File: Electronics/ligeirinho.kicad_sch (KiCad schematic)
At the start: 18 parts, among them J1 VS1838B, J10 ponte H, J11 ponte H ld motores, J12 MPU6050, J2 motor B, J3 motor A, J4 Conn_01x15, J5 VL53L0X 1, J6 VL53L0X 2, J7 VL53L0X 3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

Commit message: shore: update electronic repository
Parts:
- removed BT1: Battery_Cell, symbol Device:Battery_Cell
- added J8: bateria, symbol Connector:Conn_01x02_Pin
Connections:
- net 2s: now also J8.1 (Pin_1)
- net GND: now also J8.2 (Pin_2)
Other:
- moved on the sheet: J2, J3
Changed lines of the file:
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@@
+    (stroke (width 0) (type default))
+  )
+  (wire (pts (xy 71.12 152.4) (xy 71.12 161.29))
     (stroke (width 0) (type default))
   )
@@
     (stroke (width 0) (type default))
   )
-  (wire (pts (xy 236.22 160.02) (xy 240.03 160.02))
+  (wire (pts (xy 236.22 160.02) (xy 242.57 160.02))
     (stroke (width 0) (type default) (color 0 0 0 1))
   )
@@
     (stroke (width 0) (type default))
   )
-  (wire (pts (xy 71.12 166.37) (xy 71.12 170.18))
+  (wire (pts (xy 71.12 163.83) (xy 71.12 170.18))
     (stroke (width 0) (type default))
   )
   (wire (pts (xy 93.98 170.18) (xy 105.41 170.18))
-    (stroke (width 0) (type default))
-  )
-  (wire (pts (xy 71.12 158.75) (xy 71.12 152.4))
     (stroke (width 0) (type default))
   )
@@
     )
   )
-  (global_label "2s" (shape input) (at 71.12 157.48 0) (fields_autoplaced)
-    (effects (font (size 1.27 1.27)) (justify left))
-    (property "Intersheetrefs" "${INTERSHEET_REFS}" (at 76.3428 157.48 0)
+  (global_label "2s" (shape input) (at 71.12 152.4 90) (fields_autoplaced)
+    (effects (font (size 1.27 1.27)) (justify left))
+    (property "Intersheetrefs" "${INTERSHEET_REFS}" (at 71.12 147.1772 90)
       (effects (font (size 1.27 1.27)) (justify left) hide)
     )
@@
     )
   )
-  (global_label "BO1" (shape input) (at 162.56 154.94 0) (fields_autoplaced)
-    (effects (font (size 1.27 1.27)) (justify left))
-    (property "Intersheetrefs" "${INTERSHEET_REFS}" (at 169.3552 154.94 0)
+  (global_label "BO1" (shape input) (at 171.45 157.48 0) (fields_autoplaced)
+    (effects (font (size 1.27 1.27)) (justify left))
+    (property "Intersheetrefs" "${INTERSHEET_REFS}" (at 178.2452 157.48 0)
       (effects (font (size 1.27 1.27)) (justify left) hide)
     )
@@
     )
   )
-  (global_label "GND" (shape input) (at 240.03 160.02 0) (fields_autoplaced)
-    (effects (font (size 1.27 1.27)) (justify left))
-    (property "Intersheetrefs" "${INTERSHEET_REFS}" (at 246.8857 160.02 0)
+  (global_label "GND" (shape input) (at 242.57 160.02 0) (fields_autoplaced)
+    (effects (font (size 1.27 1.27)) (justify left))
+    (property "Intersheetrefs" "${INTERSHEET_REFS}" (at 249.4257 160.02 0)
       (effects (font (size 1.27 1.27)) (justify left) hide)
     )
@@
     )
   )
-  (global_label "AO1" (shape input) (at 171.45 148.59 0) (fields_autoplaced)
-    (effects (font (size 1.27 1.27)) (justify left))
-    (property "Intersheetrefs" "${INTERSHEET_REFS}" (at 178.0638 148.59 0)
+  (global_label "AO1" (shape input) (at 171.45 143.51 0) (fields_autoplaced)
+    (effects (font (size 1.27 1.27)) (justify left))
+    (property "Intersheetrefs" "${INTERSHEET_REFS}" (at 178.0638 143.51 0)
       (effects (font (size 1.27 1.27)) (justify left) hide)
     )
@@
     )
   )
-  (global_label "AO2" (shape input) (at 171.45 151.13 0) (fields_autoplaced)
-    (effects (font (size 1.27 1.27)) (justify left))
-    (property "Intersheetrefs" "${INTERSHEET_REFS}" (at 178.0638 151.13 0)
-      (effects (font (size 1.27 1.27)) (justify left) hide)
-    )
-  )
-  (global_label "BO2" (shape input) (at 162.56 157.48 0) (fields_autoplaced)
-    (effects (font (size 1.27 1.27)) (justify left))
-    (property "Intersheetrefs" "${INTERSHEET_REFS}" (at 169.3552 157.48 0)
+  (global_label "AO2" (shape input) (at 171.45 146.05 0) (fields_autoplaced)
+    (effects (font (size 1.27 1.27)) (justify left))
+    (property "Intersheetrefs" "${INTERSHEET_REFS}" (at 178.0638 146.05 0)
+      (effects (font (size 1.27 1.27)) (justify left) hide)
+    )
+  )
+  (global_label "BO2" (shape input) (at 171.45 160.02 0) (fields_autoplaced)
+    (effects (font (size 1.27 1.27)) (justify left))
+    (property "Intersheetrefs" "${INTERSHEET_REFS}" (at 178.2452 160.02 0)
       (effects (font (size 1.27 1.27)) (justify left) hide)
     )
@@
   (hierarchical_label "XSHUT2" (shape input) (at 137.16 97.79 0) (fields_autoplaced)
     (effects (font (size 1.27 1.27)) (justify left))
+  )
+  (symbol (lib_id "Connector:Conn_01x02_Pin") (at 66.04 161.29 0) (unit 1)
+    (in_bom yes) (on_board yes) (dnp no) (fields_autoplaced)
+    (property "Reference" "J8" (at 66.675 156.21 0)
+      (effects (font (size 1.27 1.27)))
+    )
+    (property "Value" "bateria" (at 66.675 158.75 0)
+      (effects (font (size 1.27 1.27)))
+    )
+    (property "Footprint" "" (at 66.04 161.29 0)
+      (effects (font (size 1.27 1.27)) hide)
+    )
+    (property "Datasheet" "~" (at 66.04 161.29 0)
+      (effects (font (size 1.27 1.27)) hide)
+    )
+    (pin "1")
+    (pin "2")
+    (instances
+      (project "ligeirinho"
+        (path "/6b99e809-cead-4d13-a342-d8cd71257e3b"
+          (reference "J8") (unit 1)
+        )
+      )
+    )
   )
   (symbol (lib_id "Device:R") (at 149.86 100.33 0) (unit 1)
@@
     )
   )
-  (symbol (lib_id "Connector:Conn_01x02_Pin") (at 166.37 148.59 0) (unit 1)
+  (symbol (lib_id "Connector:Conn_01x02_Pin") (at 166.37 143.51 0) (unit 1)
     (in_bom yes) (on_board yes) (dnp no) (fields_autoplaced)
-    (property "Reference" "J3" (at 167.005 143.51 0)
+    (property "Reference" "J3" (at 167.005 138.43 0)
       (effects (font (size 1.27 1.27)))
     )
-    (property "Value" "motor A" (at 167.005 146.05 0)
+    (property "Value" "motor A" (at 167.005 140.97 0)
       (effects (font (size 1.27 1.27)))
     )
-    (property "Footprint" "" (at 166.37 148.59 0)
-      (effects (font (size 1.27 1.27)) hide)
-    )
-    (property "Datasheet" "~" (at 166.37 148.59 0)
+    (property "Footprint" "" (at 166.37 143.51 0)
+      (effects (font (size 1.27 1.27)) hide)
+    )
+    (property "Datasheet" "~" (at 166.37 143.51 0)
       (effects (font (size 1.27 1.27)) hide)
     )
@@
     )
   )
-  (symbol (lib_id "Connector:Conn_01x02_Pin") (at 157.48 154.94 0) (unit 1)
+  (symbol (lib_id "Connector:Conn_01x02_Pin") (at 166.37 157.48 0) (unit 1)
     (in_bom yes) (on_board yes) (dnp no)
-    (property "Reference" "J2" (at 155.575 149.86 0)
+    (property "Reference" "J2" (at 165.1 152.4 0)
       (effects (font (size 1.27 1.27)))
     )
-    (property "Value" "motor B" (at 158.115 152.4 0)
+    (property "Value" "motor B" (at 167.005 154.94 0)
       (effects (font (size 1.27 1.27)))
     )
-    (property "Footprint" "" (at 157.48 154.94 0)
-      (effects (font (size 1.27 1.27)) hide)
-    )
-    (property "Datasheet" "~" (at 157.48 154.94 0)
+    (property "Footprint" "" (at 166.37 157.48 0)
+      (effects (font (size 1.27 1.27)) hide)
+    )
+    (property "Datasheet" "~" (at 166.37 157.48 0)
       (effects (font (size 1.27 1.27)) hide)
     )
@@
         )
       )
-    )
-  )
-  (symbol (lib_id "Device:Battery_Cell") (at 71.12 163.83 0) (unit 1)
-    (in_bom yes) (on_board yes) (dnp no) (fields_autoplaced)
-    (property "Reference" "BT1" (at 74.93 160.7185 0)
-      (effects (font (size 1.27 1.27)) (justify left))
-    )
-    (property "Value" "Battery_Cell" (at 74.93 163.2585 0)
-      (effects (font (size 1.27 1.27)) (justify left))
-    )
-    (property "Footprint" "" (at 71.12 162.306 90)
-      (effects (font (size 1.27 1.27)) hide)
-    )
-    (property "Datasheet" "~" (at 71.12 162.306 90)
-      (effects (font (size 1.27 1.27)) hide)
-    )
-    (pin "1")
-    (pin "2")
-    (instances
-      (project "ligeirinho"
-        (path "/6b99e809-cead-4d13-a342-d8cd71257e3b"
-          (reference "BT1") (unit 1)
-        )
-      )

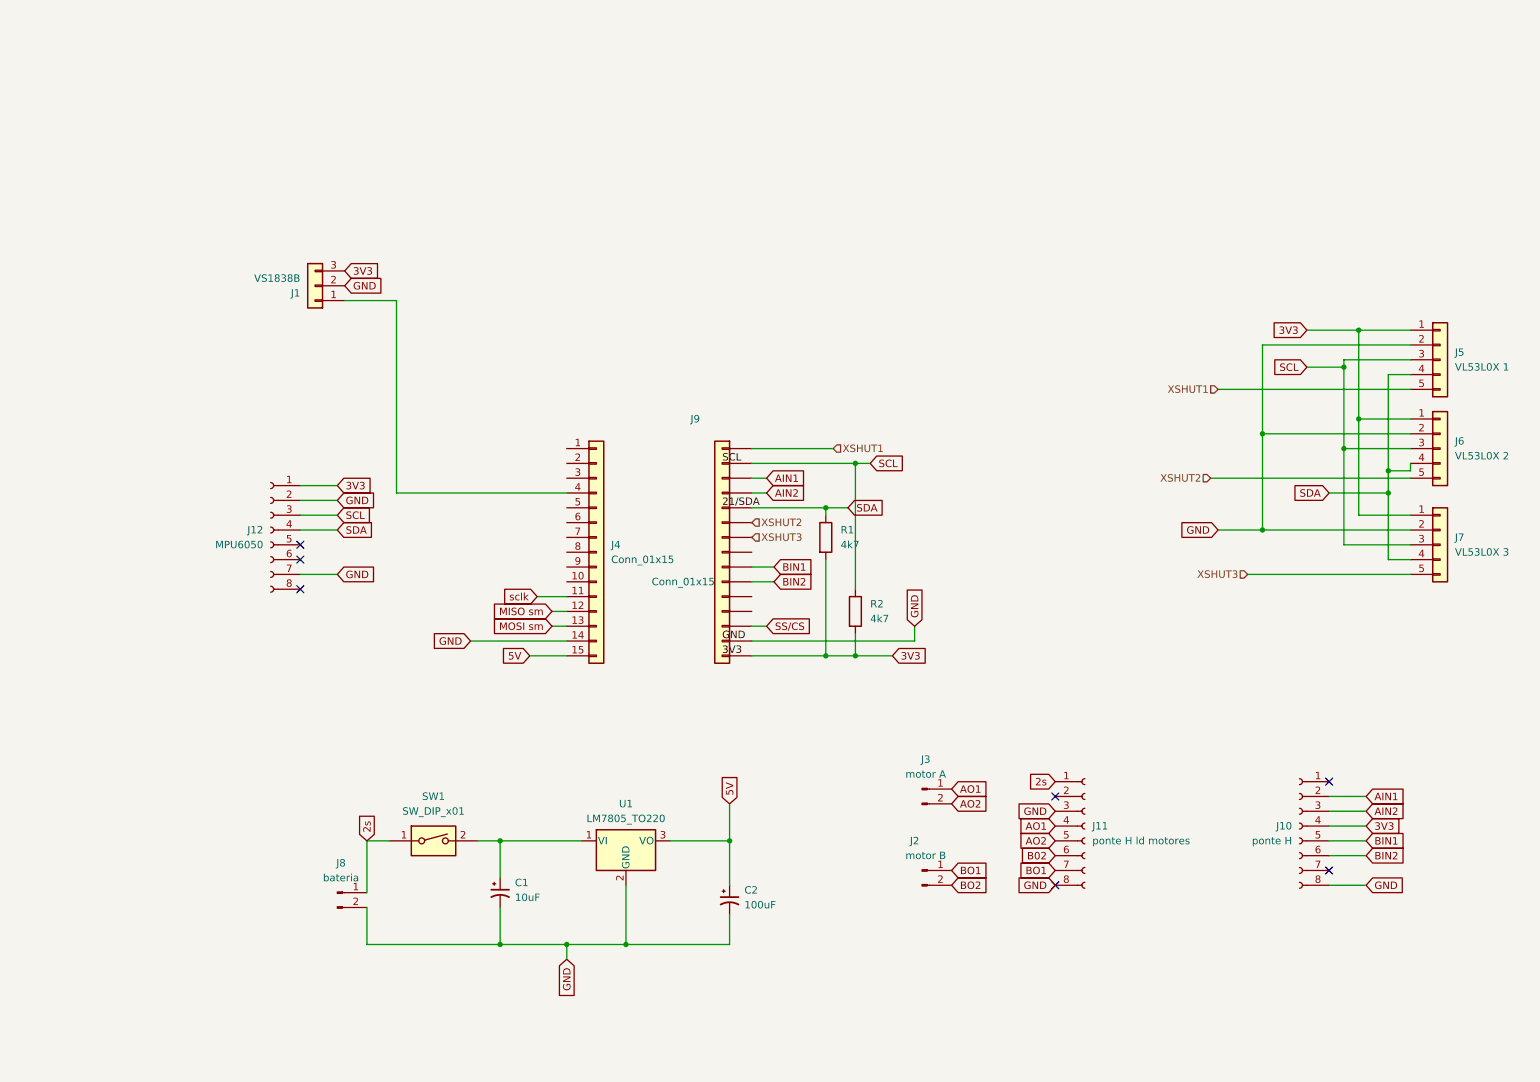
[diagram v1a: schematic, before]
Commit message: shore: organized tags, add footprints and esp32 schematic
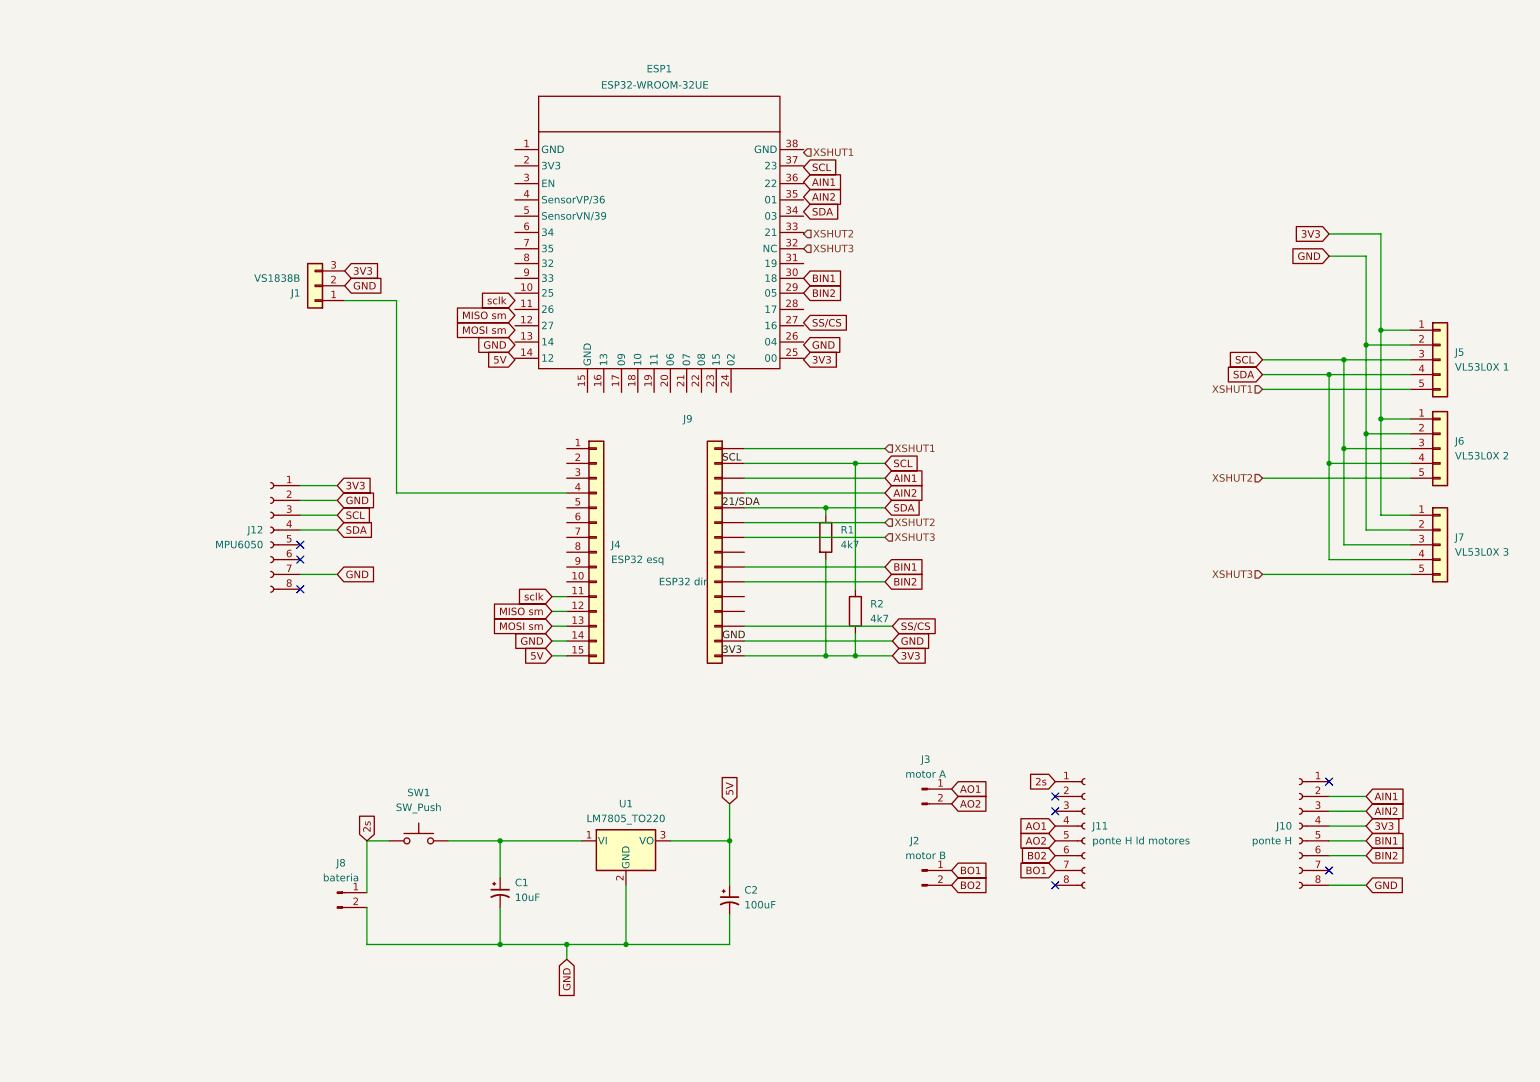
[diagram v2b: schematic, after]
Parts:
- removed SW1: SW_DIP_x01, symbol Switch:SW_DIP_x01
- added ESP1: ESP32-WROOM­32UE, RF_Module:ESP32-WROOM-32, symbol espSMD:ESP32-WROOM­32UE
- added SW1: SW_Push, Button_Switch_THT:Nidec_Copal_SH-7010C, symbol Switch:SW_Push
- J4: value Conn_01x15 -> ESP32 esq; footprint (none) -> RF_Module:ESP32-WROOM-32
- J9: value Conn_01x15 -> ESP32 dir; footprint (none) -> RF_Module:ESP32-WROOM-32
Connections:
- net 2s: now also SW1.1
- net BIN1: now also ESP1.30 (18)
- net BIN2: now also ESP1.29 (05)
- net GND: no longer J11.3 (Pin_3), J11.8 (Pin_8)
- net XSHUT3: now also ESP1.32 (NC)
- net at C1.1, U1.1 (VI): now also SW1.2
- no-connect marks 7 -> 8
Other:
- moved on the sheet: J9
